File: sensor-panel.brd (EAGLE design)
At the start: 49.2 x 49.5 mm, 80 parts

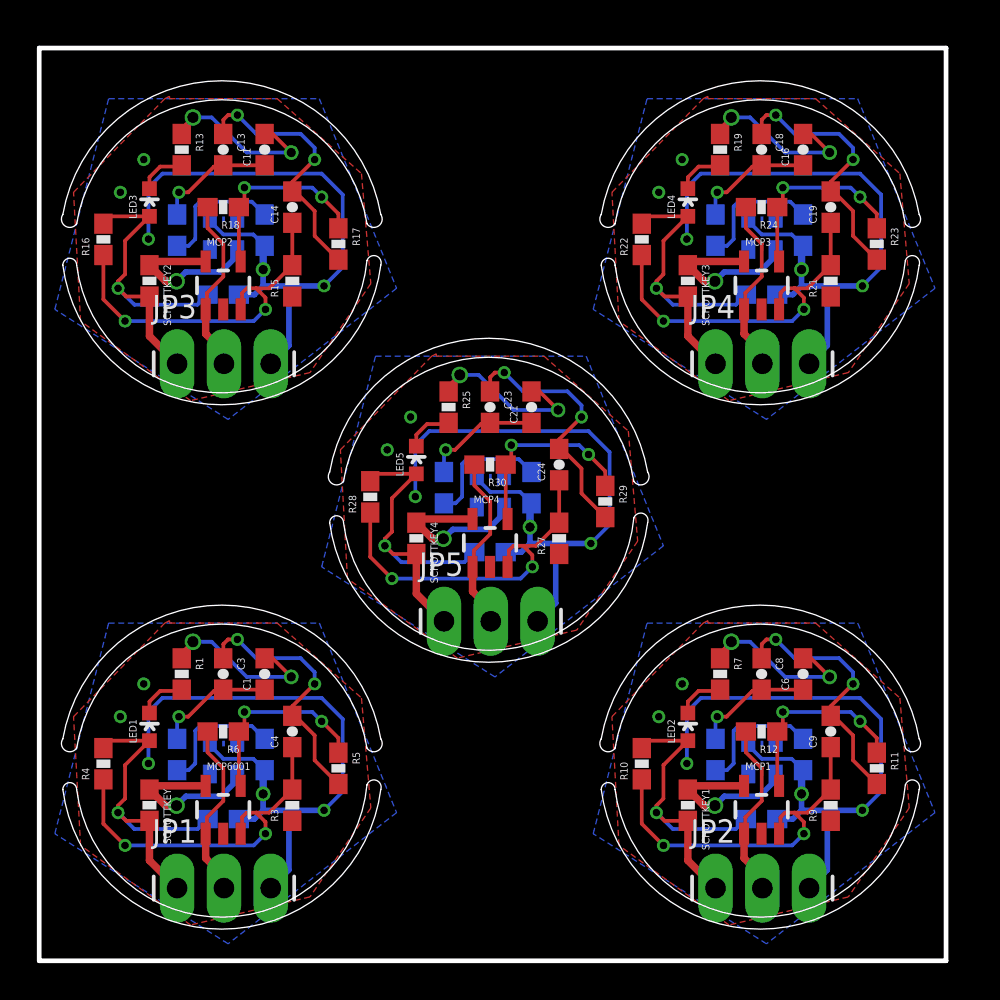
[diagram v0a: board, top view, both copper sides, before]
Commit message: sensor: correct schematic and refine layout
1. Replace fake schottkey with a *real* one.
2. Refine polygon.
3. Refine dimension.
4. Refine panel.
5. Add more blowholes (vias).
6. Slightly refine some wires.
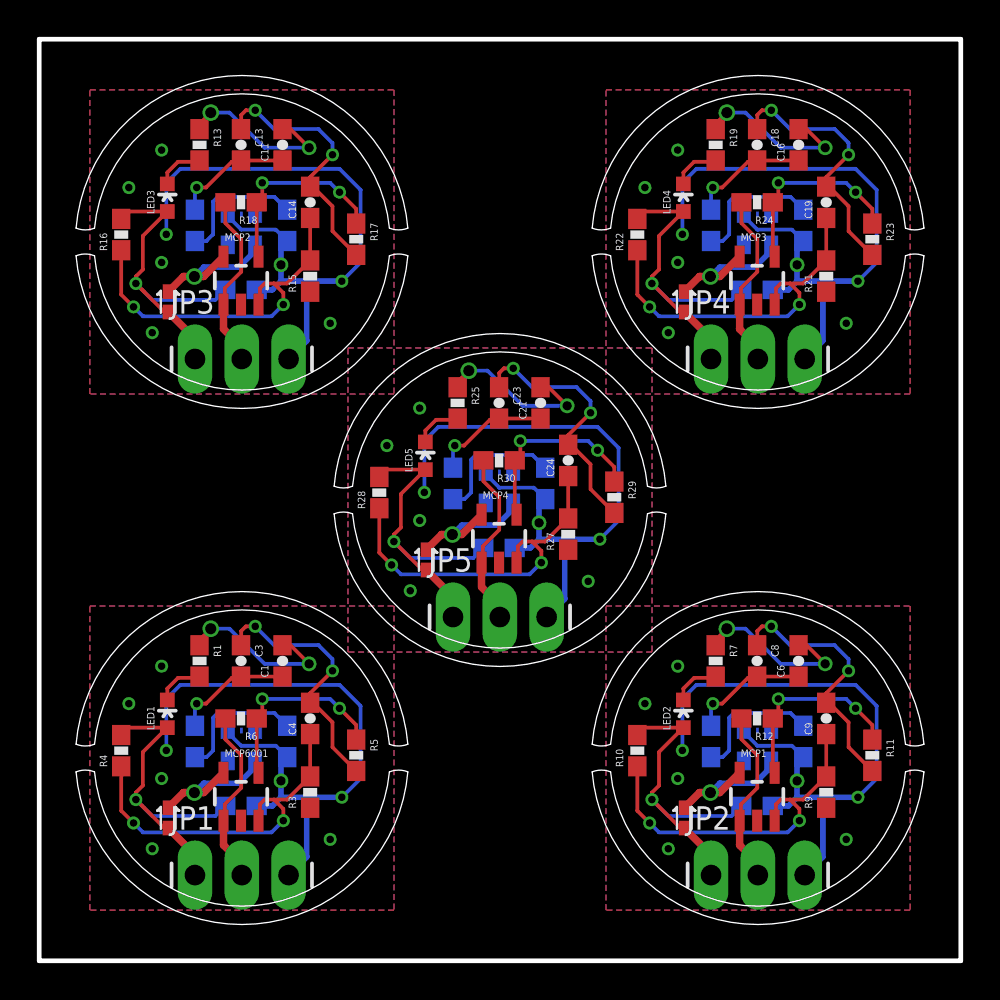
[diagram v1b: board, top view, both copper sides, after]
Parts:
- removed SCHOTTKEY, SCHOTTKEY1, SCHOTTKEY2, SCHOTTKEY3, SCHOTTKEY4: 0, SparkFun-Resistors:0603-RES
- added D1, D2, D3, D4, D5: RB751, SparkFun-DiscreteSemi:SOD-523
- moved R2 1.41 mm to (13.5, 11.9)
- moved R14 1.25 mm to (13.5, 39.9)
- moved APDS1 1.20 mm to (10.9, 11.7)
- moved C4 1.20 mm to (14.7, 13.2)
- moved C5 1.20 mm to (10.9, 8.40)
- moved LED1 1.20 mm to (6.95, 13.4)
- moved MCP6001 1.20 mm to (10.9, 8.90)
- moved R3 1.20 mm to (14.7, 9.15)
- moved R4 1.20 mm to (4.45, 11.4)
- moved R5 1.20 mm to (17.2, 11.2)
- moved R6 1.20 mm to (10.9, 13.2)
- moved C2 1.20 mm to (8.45, 11.9)
- moved JP1 1.20 mm to (8.45, 4.65)
- moved C1 1.20 mm to (13.2, 16.3)
- moved C3 1.20 mm to (10.9, 16.3)
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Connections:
- net VCC: now also D2.A; no longer SCHOTTKEY.2
- net VCC1: now also D3.A; no longer SCHOTTKEY1.2
- net VCC2: now also D4.A; no longer SCHOTTKEY2.2
- net VCC3: now also D5.A; no longer SCHOTTKEY3.2
- net VCC4: now also D1.A; no longer SCHOTTKEY4.2
- net VDD: now also D2.C; no longer SCHOTTKEY.1
- net VDD1: now also D3.C; no longer SCHOTTKEY1.1
- net VDD2: now also D4.C; no longer SCHOTTKEY2.1
- net VDD3: now also D5.C; no longer SCHOTTKEY3.1
- net VDD4: now also D1.C; no longer SCHOTTKEY4.1
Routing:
- net VDD2: track 9.16 -> 7.98 mm
- net VDD: track 9.16 -> 7.98 mm
- net VDD3: track 9.16 -> 7.98 mm
- net VDD4: track 9.16 -> 7.98 mm
- net VDD1: track 9.16 -> 7.98 mm
- net VCC4: track 18.9 -> 18.3 mm
- net VCC1: track 18.9 -> 18.3 mm
- net VCC: track 18.9 -> 18.3 mm
- net VCC3: track 18.9 -> 18.3 mm
- net VCC2: track 18.9 -> 18.3 mm
- net GND4: track 44.1 -> 44.7 mm, vias 7 -> 10
- net GND2: track 44.1 -> 44.7 mm, vias 7 -> 10
- net GND: track 44.1 -> 44.7 mm, vias 7 -> 10
- net GND3: track 44.1 -> 44.7 mm, vias 7 -> 10
- net GND1: track 44.1 -> 44.7 mm, vias 7 -> 10
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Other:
- board size 49.2 x 49.5 mm -> 50 x 50 mm

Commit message: sensor: update pcb layout
Mainly correct LED position and work mechanism.
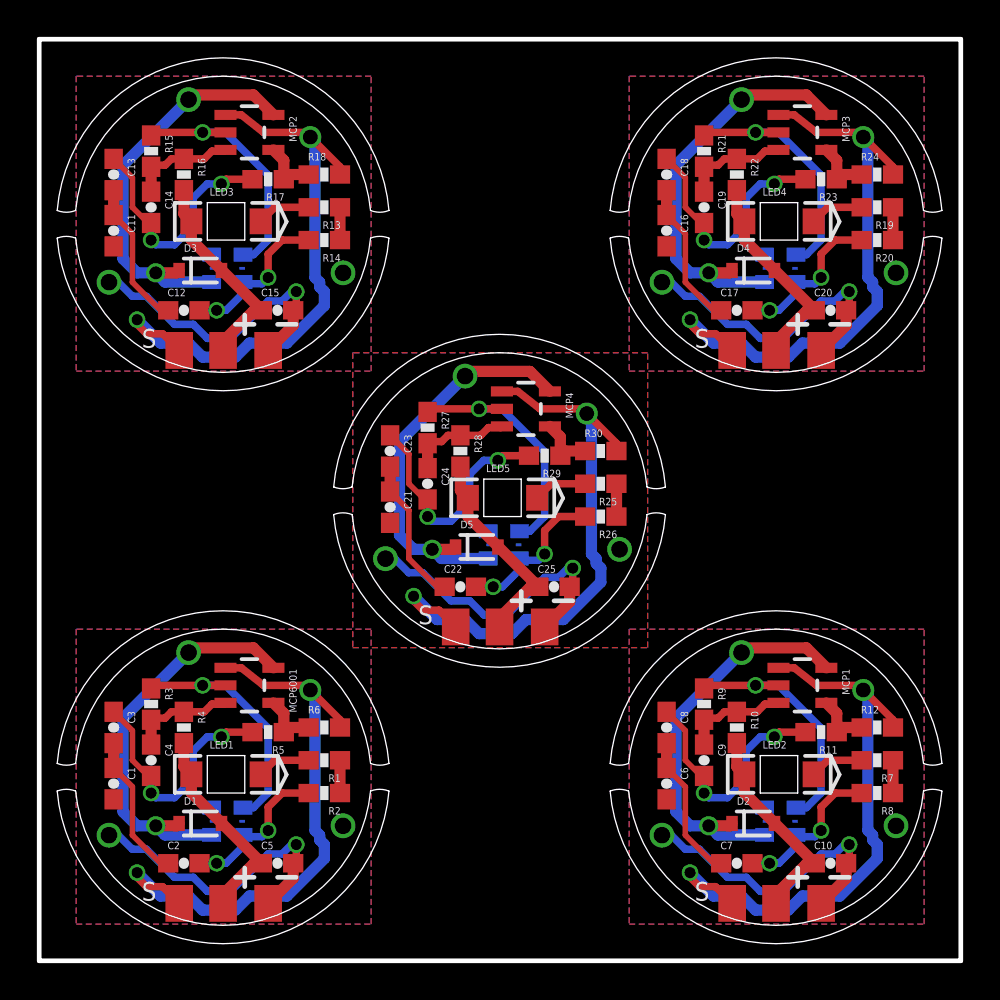
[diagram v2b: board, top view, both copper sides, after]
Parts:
- removed JP1, JP2, JP3, JP4, JP5: (no value), SparkFun-Connectors:1X03_LONGPADS
- added GND1, GND2, GND3, GND4, GND5, OUT1, OUT2, OUT3, OUT4, OUT5, VCC1, VCC2, VCC3, VCC4, VCC5: M01SMD-4.5X1.5, SparkFun-Connectors:PAD-1.5X4.5
- D1, D2, D3, D4, D5: value RB751 -> BAT20JFILM; device SparkFun-DiscreteSemi:SOD-523 -> SparkFun-DiscreteSemi:SOD-323
- LED1, LED2, LED3, LED4, LED5: device SparkFun-LED:LED-0603 -> librae:LED-1206-REVERSE-MOUNT
- moved D3 39.6 mm to (8.74, 37.5), turned to 0 degrees
- moved D4 31.8 mm to (38.7, 37.5), turned to 0 degrees
- moved D2 31.7 mm to (38.7, 7.45), turned to 0 degrees
- moved D1 18.8 mm to (8.74, 7.45), turned to 0 degrees
- moved D5 17.4 mm to (23.7, 22.5), turned to 0 degrees
- moved C1 11.3 mm to (4.04, 9.61), turned to 270 degrees
- moved R15 11.0 mm to (6.07, 43.9), turned to 270 degrees
- moved R7 10.3 mm to (45.5, 10.9), turned to 180 degrees
- moved C11 10.3 mm to (4.04, 39.6), turned to 270 degrees
- moved C21 9.93 mm to (19.0, 24.6), turned to 270 degrees
- moved R3 9.86 mm to (6.07, 13.9), turned to 270 degrees
- moved C6 9.78 mm to (34.0, 9.61), turned to 270 degrees
- moved R27 9.57 mm to (21.1, 28.9), turned to 270 degrees
- moved R21 9.48 mm to (36.1, 43.9), turned to 270 degrees
- moved R19 9.40 mm to (45.5, 40.9), turned to 180 degrees
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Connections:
- net GND: now also GND1.P$1; no longer JP1.3
- net GND1: now also GND2.P$1; no longer JP2.3
- net GND2: now also GND3.P$1; no longer JP3.3
- net GND3: now also GND4.P$1; no longer JP4.3
- net GND4: now also GND5.P$1; no longer JP5.3
- net OUT: now also OUT1.P$1; no longer JP1.2
- net OUT1: now also OUT2.P$1; no longer JP2.2
- net OUT2: now also OUT3.P$1; no longer JP3.2
- net OUT3: now also OUT4.P$1; no longer JP4.2
- net OUT4: now also OUT5.P$1; no longer JP5.2
- net VCC: now also D1.2, VCC1.P$1; no longer D2.A, JP1.1
- net VCC1: now also D2.2, VCC2.P$1; no longer D3.A, JP2.1
- net VCC2: now also D3.2, VCC3.P$1; no longer D4.A, JP3.1
- net VCC3: now also D4.2, VCC4.P$1; no longer D5.A, JP4.1
- net VCC4: now also D5.2, VCC5.P$1; no longer D1.A, JP5.1
- net VDD: now also D1.1; no longer D2.C
- net VDD1: now also D2.1; no longer D3.C
- net VDD2: now also D3.1; no longer D4.C
- net VDD3: now also D4.1; no longer D5.C
- net VDD4: now also D5.1; no longer D1.C
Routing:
- net OUT4: track 9.66 -> 32.5 mm, vias 0 -> 2
- net OUT3: track 9.66 -> 32.5 mm, vias 0 -> 2
- net OUT2: track 9.66 -> 32.5 mm, vias 0 -> 2
- net OUT1: track 9.66 -> 32.5 mm, vias 0 -> 2
- net OUT: track 9.66 -> 32.5 mm, vias 0 -> 2
- net N$29: track 19.9 -> 5.76 mm, vias 2 -> 0
- net N$11: track 19.9 -> 5.76 mm, vias 2 -> 0
- net N$10: track 19.9 -> 5.76 mm, vias 2 -> 0
- net N$23: track 19.9 -> 5.76 mm, vias 2 -> 0
- net N$17: track 19.9 -> 5.76 mm, vias 2 -> 0
- net VDD4: track 7.98 -> 21.9 mm, vias 1 -> 2
- net VDD: track 7.98 -> 21.9 mm, vias 1 -> 2
- net VDD2: track 7.98 -> 21.9 mm, vias 1 -> 2
- net VDD1: track 7.98 -> 21.9 mm, vias 1 -> 2
- net VDD3: track 7.98 -> 21.9 mm, vias 1 -> 2
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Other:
- outline, holes or cut-outs redrawn
- board text added: "S"
- board text removed: "APDS1"
- board text removed: "C1"
- board text removed: "C2"
- board text removed: "C3"
- board text removed: "C4"
- board text removed: "C5"
- board text removed: "JP1"
- board text removed: "LED1"
- board text removed: "MCP6001"
- board text removed: "R1"
- board text removed: "R2"
- board text removed: "R3"
- board text removed: "R4"
- board text removed: "R5"
- board text removed: "R6"
- board text removed: "SCHOTTKEY"
